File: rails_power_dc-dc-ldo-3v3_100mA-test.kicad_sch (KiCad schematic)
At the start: 5 parts, among them J101 Conn_02x03_Odd_Even

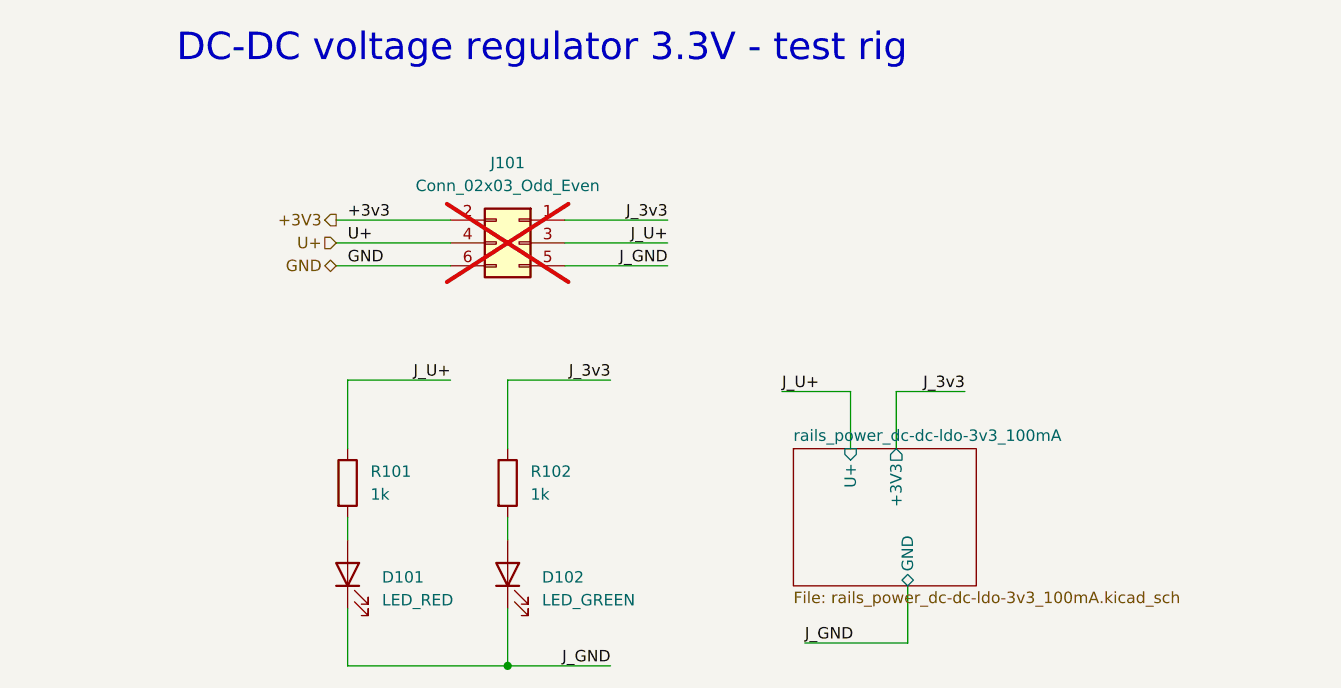
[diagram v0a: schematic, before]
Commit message: Fix - DRC errors in LDO test schematics
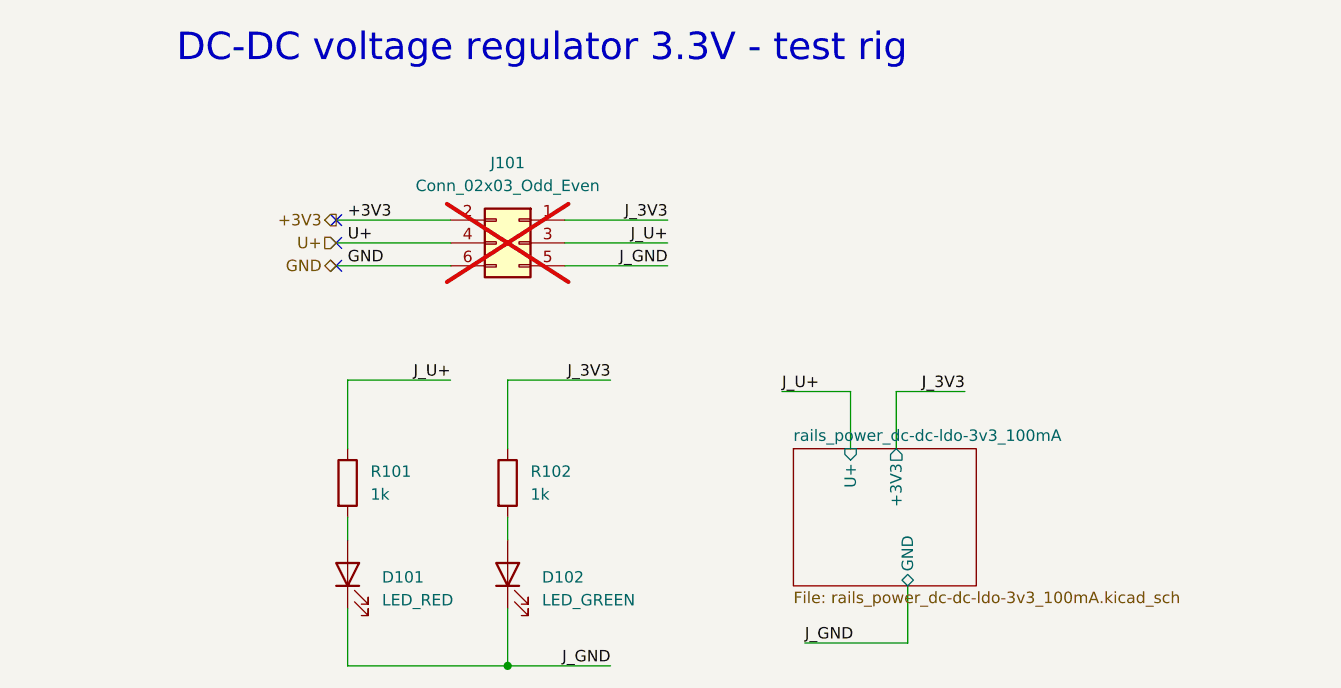
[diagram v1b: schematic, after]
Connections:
- net J_3v3 renamed J_3V3
- no-connect marks 0 -> 3
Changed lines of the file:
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@@
 		(color 0 0 0 0)
+	)
+	(no_connect
+		(at 41.91 46.99)
+	)
+	(no_connect
+		(at 41.91 44.45)
+	)
+	(no_connect
+		(at 41.91 49.53)
 	)
 	(wire
@@
 	(label "U+"
 		(at 43.18 46.99 0)
-		(fields_autoplaced yes)
 		(effects
 			(font
@@
 	(label "J_GND"
 		(at 78.74 49.53 180)
-		(fields_autoplaced yes)
 		(effects
 			(font
@@
 	(label "J_U+"
 		(at 91.44 63.5 0)
-		(fields_autoplaced yes)
 		(effects
 			(font
@@
 	(label "J_U+"
 		(at 54.61 62.23 180)
-		(fields_autoplaced yes)
 		(effects
 			(font
@@
 	(label "GND"
 		(at 43.18 49.53 0)
-		(fields_autoplaced yes)
 		(effects
 			(font
@@
 	(label "J_GND"
 		(at 72.39 93.98 180)
-		(fields_autoplaced yes)
 		(effects
 			(font
@@
 	(label "J_GND"
 		(at 93.98 91.44 0)
-		(fields_autoplaced yes)
-		(effects
-			(font
-				(size 1.27 1.27)
-			)
-			(justify left bottom)
-		)
-	)
-	(label "J_3v3"
+		(effects
+			(font
+				(size 1.27 1.27)
+			)
+			(justify left bottom)
+		)
+	)
+	(label "J_3V3"
 		(at 111.76 63.5 180)
-		(fields_autoplaced yes)
-		(effects
-			(font
-				(size 1.27 1.27)
-			)
-			(justify right bottom)
-		)
-	)
-	(label "J_3v3"
+		(effects
+			(font
+				(size 1.27 1.27)
+			)
+			(justify right bottom)
+		)
+	)
+	(label "J_3V3"
 		(at 78.74 44.45 180)
-		(fields_autoplaced yes)
-		(effects
-			(font
-				(size 1.27 1.27)
-			)
-			(justify right bottom)
-		)
-	)
-	(label "J_3v3"
+		(effects
+			(font
+				(size 1.27 1.27)
+			)
+			(justify right bottom)
+		)
+	)
+	(label "J_3V3"
 		(at 72.39 62.23 180)
-		(fields_autoplaced yes)
-		(effects
-			(font
-				(size 1.27 1.27)
-			)
-			(justify right bottom)
-		)
-	)
-	(label "+3v3"
+		(effects
+			(font
+				(size 1.27 1.27)
+			)
+			(justify right bottom)
+		)
+	)
+	(label "+3V3"
 		(at 43.18 44.45 0)
-		(fields_autoplaced yes)
 		(effects
 			(font
@@
 	(label "J_U+"
 		(at 78.74 46.99 180)
-		(fields_autoplaced yes)
 		(effects
 			(font
@@
 		(shape output)
 		(at 41.91 44.45 180)
-		(fields_autoplaced yes)
 		(effects
 			(font
@@
 		(shape bidirectional)
 		(at 41.91 49.53 180)
-		(fields_autoplaced yes)
 		(effects
 			(font
@@
 		(shape input)
 		(at 41.91 46.99 180)
-		(fields_autoplaced yes)
-		(effects
-			(font
+		(effects
+			(font
